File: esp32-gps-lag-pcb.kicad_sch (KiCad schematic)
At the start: 5 parts, among them J1 GPS UART, J2 eInk display, SW1 SW_Push, U1 ESP32-DevKitC

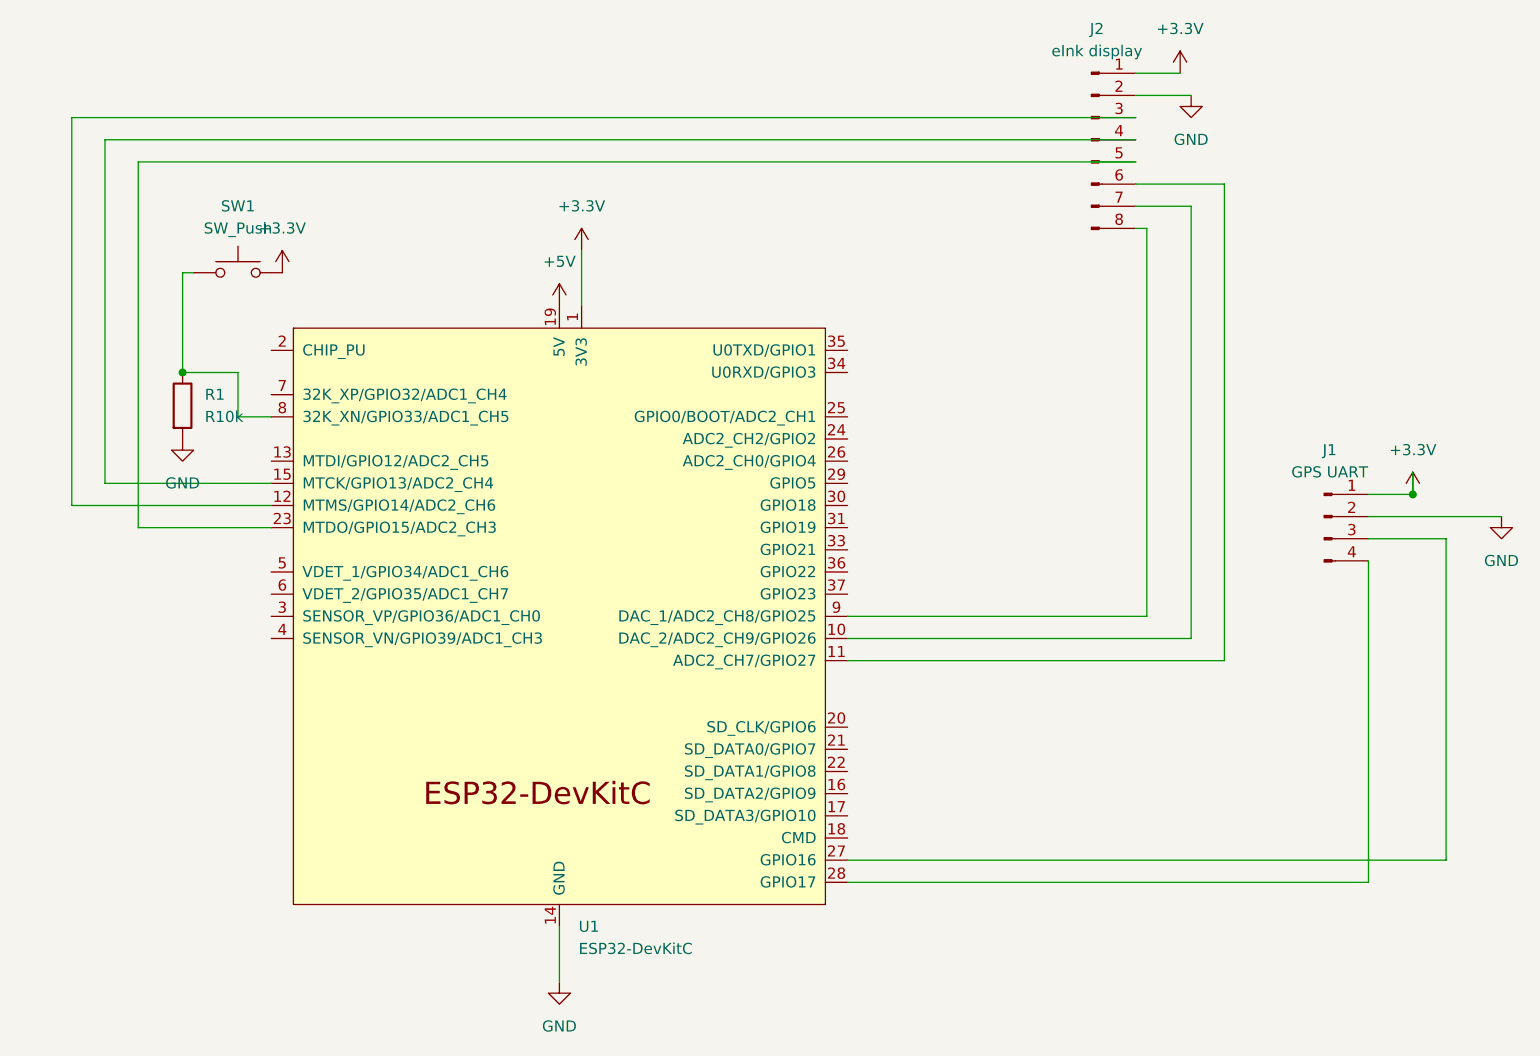
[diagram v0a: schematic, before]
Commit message: Battery capacity measurement, new GNSS module, etc.
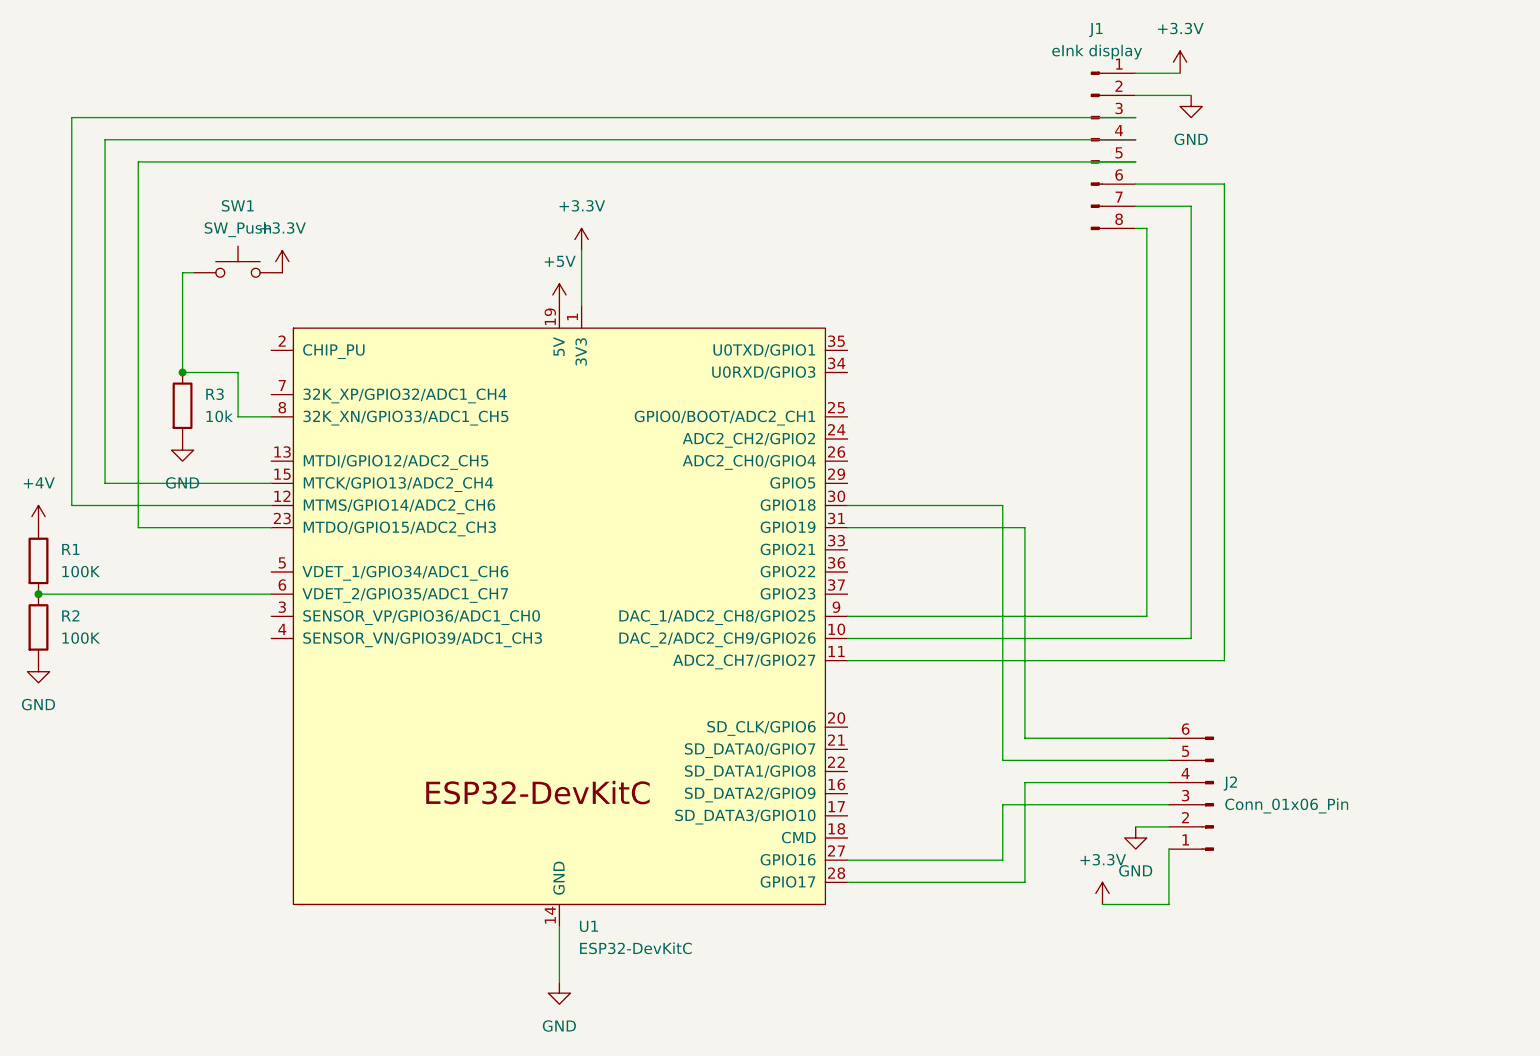
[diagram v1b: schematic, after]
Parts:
- added R1, R2: 100K, Resistor_THT:R_Axial_DIN0204_L3.6mm_D1.6mm_P5.08mm_Horizontal, symbol Device:R
- J2: renamed from J1; value GPS UART -> Conn_01x06_Pin; footprint Connector_PinHeader_2.54mm:PinHeader_1x04_P2.54mm_Vertical -> Connector_PinHeader_2.54mm:PinHeader_1x06_P2.54mm_Vertical; symbol Connector:Conn_01x04_Pin -> Connector:Conn_01x06_Pin
- R3: renamed from R1; value R10k -> 10k
- renumbered J2 to J1
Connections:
- net GND: now also R2.2
- net at U1.30 (GPIO18): now also J2.5 (Pin_5)
- net at U1.31 (GPIO19): now also J2.6 (Pin_6)
- net at U1.6 (VDET_2/GPIO35/ADC1_CH7): now also R1.2, R2.1
- new net +4V: R1.1
